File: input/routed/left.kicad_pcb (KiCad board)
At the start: 2 copper layers, 90 x 71 mm, 44 parts, among them T1 Flactyl 4.0 (left)

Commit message: Fix
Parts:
- SS1: value (none) -> SW-TH_MSK12C02-HB-1
- T1: value Flactyl 4.0 (left) -> Flactyl 4.1 (left)
- turned SS1 to 180 degrees

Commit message: 4.1
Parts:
- moved H6 15.7 mm to (60.5, -39.5)
- moved H5 8.50 mm to (63.0, -14.0)
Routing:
- net R2: track 122.7 -> 124.1 mm
- net C0: track 122.1 -> 122.9 mm
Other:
- outline, holes or cut-outs redrawn

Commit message: Update routed
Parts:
- removed H6: , MountingHole_2.2mm_M2
- T1: value Flactyl 4.1 (left) -> Flactyl 4.2 (left)
- moved D1 79.4 mm to (75.6, -42.4), turned to 0 degrees
- moved D2 79.4 mm to (75.6, -25.4), turned to 0 degrees
- moved D16 76.6 mm to (68.4, -13.6)
- moved S1 72.8 mm to (72.0, -45.0), turned to 0 degrees
- moved S2 72.8 mm to (72.0, -28.0), turned to 0 degrees
- moved H1 60.1 mm to (60.5, -39.5)
- moved H5 54.3 mm to (9.00, -8.50)
- moved D3 52.9 mm to (4.00, -55.0)
- moved S4 38.5 mm to (0.00, -17.0)
- moved S5 38.5 mm to (0.00, 0.00)
- moved S12 34.0 mm to (54.0, -48.0), turned to 0 degrees
- moved S3 34.0 mm to (0.00, -34.0)
- moved S6 34.0 mm to (18.0, -51.0)
- moved S9 34.0 mm to (36.0, -54.0), turned to 0 degrees
- moved D11 27.6 mm to (32.4, -39.6), turned to 180 degrees
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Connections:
- D1 pad 2: C0R0D -> C4_R0D
- D10 pad 2: C3R0D -> C2_R0D
- D11 pad 2: C3R1D -> C2_R1D
- D12 pad 2: C3R2D -> C2_R2D
- D13 pad 2: C4R0D -> C3_R0D
- D14 pad 2: C4R1D -> C3_R1D
- D15 pad 2: C4R2D -> C3_R2D
- D16 pad 1: R3 -> R2
- D16 pad 2: C0R3D -> C4_R2D
- D2 pad 2: C0R1D -> C4_R1D
- D3 pad 1: R2 -> R3
- D3 pad 2: C0R2D -> C0R3D
- D4 pad 2: C1R0D -> C0_R0D
- D5 pad 2: C1R1D -> C0_R1D
- D6 pad 2: C1R2D -> C0_R2D
- D7 pad 2: C2R0D -> C1_R0D
- D8 pad 2: C2R1D -> C1_R1D
- D9 pad 2: C2R2D -> C1_R2D
- S1 pad 1: C0R0D -> C4_R0D
- S1 pad 2: C0 -> C4
- S10 pad 1: C3R0D -> C2_R1D
- S10 pad 2: C3 -> C2
- S10 pad 3: C3R0D -> C2_R1D
- S10 pad 4: C3 -> C2
- S11 pad 1: C3R1D -> C2_R2D
- S11 pad 2: C3 -> C2
- S11 pad 3: C3R1D -> C2_R2D
- S11 pad 4: C3 -> C2
- S12 pad 1: C3R2D -> C3_R0D
- S12 pad 3: C3R2D -> C3_R0D
- S13 pad 1: C4R0D -> C3_R1D
- S13 pad 2: C4 -> C3
- S14 pad 1: C4R1D -> C3_R2D
- S14 pad 2: C4 -> C3
- S15 pad 1: C4R2D -> C4_R2D
- S15 pad 3: C4R2D -> C4_R2D
- S2 pad 1: C0R1D -> C4_R1D
- S2 pad 2: C0 -> C4
- S3 pad 1: C0R2D -> C0_R0D
- S3 pad 3: C0R2D -> C0_R0D
- S4 pad 1: C1R0D -> C0_R1D
- S4 pad 2: C1 -> C0
- S4 pad 3: C1R0D -> C0_R1D
- S4 pad 4: C1 -> C0
- S5 pad 1: C1R1D -> C0_R2D
- S5 pad 2: C1 -> C0
- S5 pad 3: C1R1D -> C0_R2D
- S5 pad 4: C1 -> C0
- S6 pad 1: C1R2D -> C1_R0D
- S6 pad 3: C1R2D -> C1_R0D
- S7 pad 1: C2R0D -> C1_R1D
- S7 pad 2: C2 -> C1
- S7 pad 3: C2R0D -> C1_R1D
- S7 pad 4: C2 -> C1
- S8 pad 1: C2R1D -> C1_R2D
- S8 pad 2: C2 -> C1
- S8 pad 3: C2R1D -> C1_R2D
- S8 pad 4: C2 -> C1
- S9 pad 1: C2R2D -> C2_R0D
- S9 pad 3: C2R2D -> C2_R0D
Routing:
- net C4_R0D: track 0.00 -> 20.7 mm
- net C4R0D: track 20.7 -> 0.00 mm
- net C4_R1D: track 0.00 -> 9.80 mm
- net C4R1D: track 9.80 -> 0.00 mm
- net C1_R1D: track 0.00 -> 3.77 mm
- net C1R1D: track 3.77 -> 0.00 mm
- net C2_R1D: track 0.00 -> 3.77 mm
- net C2R1D: track 3.77 -> 0.00 mm
- net C2_R2D: track 0.00 -> 3.77 mm
- net C2R2D: track 3.77 -> 0.00 mm
- net C1_R0D: track 0.00 -> 3.77 mm
- net C1R0D: track 3.77 -> 0.00 mm
- net C0_R2D: track 0.00 -> 3.77 mm
- net C0_R0D: track 0.00 -> 3.77 mm
- net C0R2D: track 3.77 -> 0.00 mm
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
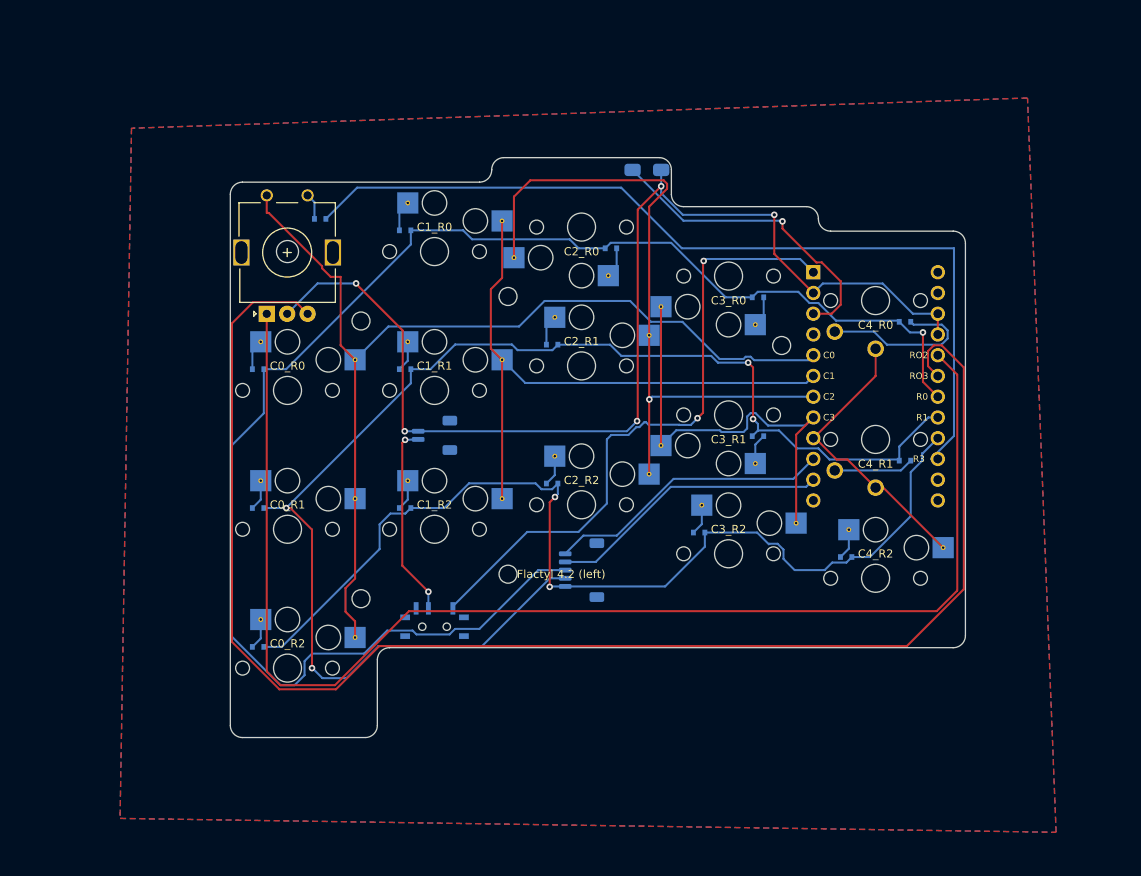
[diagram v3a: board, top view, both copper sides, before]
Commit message: Routed left
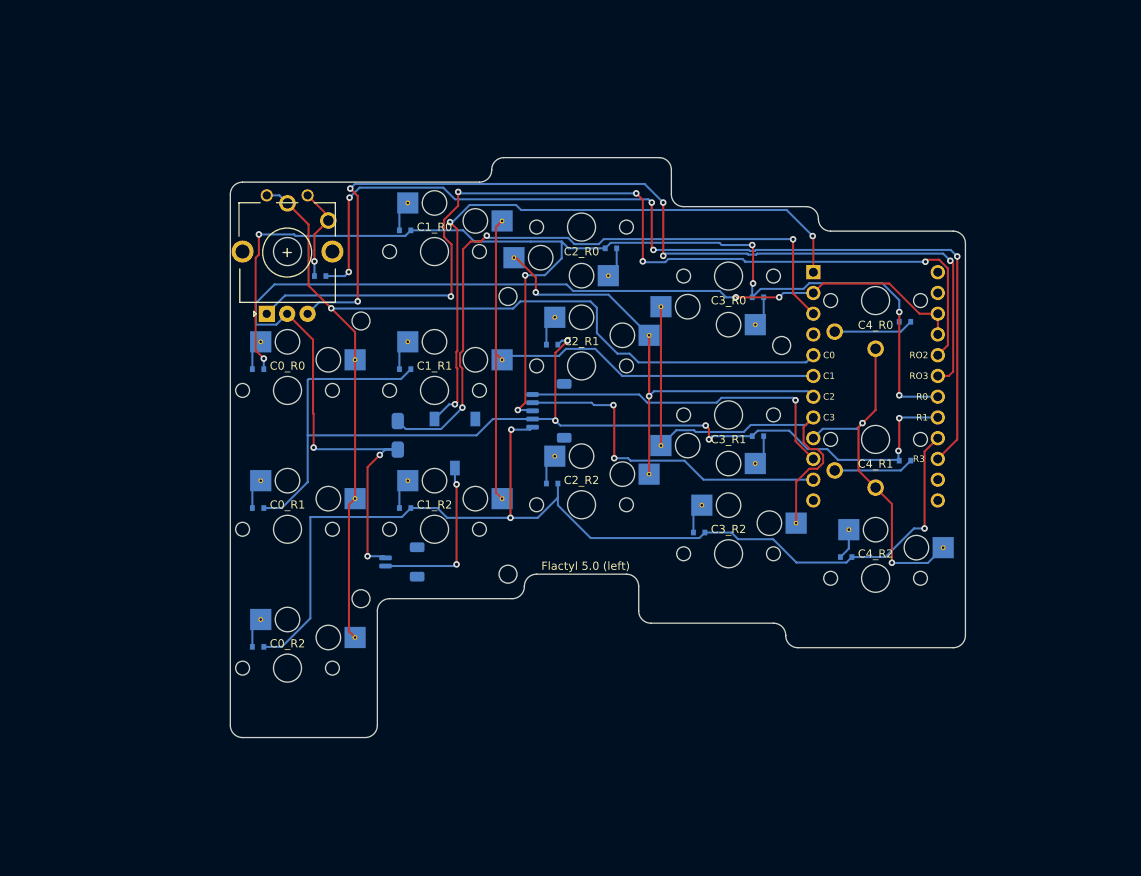
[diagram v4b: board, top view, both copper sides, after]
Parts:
- SS1: value SW-TH_MSK12C02-HB-1 -> SW-SMD_SS-3235D-03-L2.00; footprint easyeda:SW-TH_MSK12C02-HB-1 -> SW-SMD_SS-3235D-03-L2.00; moved to B.Cu
- T1: value Flactyl 4.2 (left) -> Flactyl 5.0 (left)
- moved SB1 44.6 mm to (13.5, -28.5), turned to 90 degrees
- moved SS1 22.1 mm to (20.5, -27.5), turned to 0 degrees
- moved JC1 19.9 mm to (32.0, -31.5)
- moved JB1 16.0 mm to (14.0, -13.0)
- moved D3 7.00 mm to (4.00, -48.0)
- moved T1 3.16 mm to (36.5, -12.5)
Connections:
- net C0R3D renamed C0_R3D
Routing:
- net P3: track 183.5 -> 118.5 mm, vias 0 -> 5
- net P2: track 163.6 -> 117.4 mm, vias 0 -> 5
- net RST: track 38.3 -> 81.0 mm, vias 1 -> 3
- net R0: track 188.5 -> 149.0 mm, vias 1 -> 8
- net R1: track 164.4 -> 131.2 mm, vias 4 -> 6
- net C2: track 83.9 -> 66.6 mm, vias 1 -> 2
- net C1: track 74.8 -> 91.2 mm
- net C4_R0D: track 20.7 -> 9.80 mm
- net R3: track 109.4 -> 119.7 mm, vias 0 -> 5
- net C0_R3D: track 3.23 -> 11.6 mm, vias 0 -> 1
- net C6: track 34.6 -> 42.0 mm, vias 0 -> 2
- net C4: track 35.6 -> 42.6 mm, vias 0 -> 2
- net C5: track 35.2 -> 41.1 mm, vias 0 -> 1
- net R2: track 124.1 -> 129.9 mm, vias 2 -> 3
- net GND: track 138.6 -> 142.8 mm
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- removed copper zone on B.Cu, net GND
- removed copper zone on F.Cu, net GND
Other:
- outline, holes or cut-outs redrawn

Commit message: V5 pcbs
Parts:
- moved SS1 0.25 mm to (20.5, -27.2)
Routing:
- net R1: track 131.2 -> 120.5 mm
- added copper zone on B.Cu, net GND
- added copper zone on F.Cu, net GND

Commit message: PCB 5.1
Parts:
- T1: value Flactyl 5.0 (left) -> Flactyl 5.1 (left)
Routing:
- net C1: track 91.2 -> 75.9 mm
- net C0: track 124.8 -> 128.6 mm
- net GND: track 142.8 -> 144.8 mm
- net P3: track 118.5 -> 117.3 mm
- net R0: track 149.0 -> 149.9 mm
